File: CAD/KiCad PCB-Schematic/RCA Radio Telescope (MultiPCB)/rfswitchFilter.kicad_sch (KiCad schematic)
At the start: 15 parts, among them J10 FILTER_OUT, J9 ANT, U3 SKY13588-460LF, U4 SKY13588-460LF, U5 SN74AVC2T244DQER, U6 MIC5365-1.8YC5-TR, U7 MIC5365-3.3YC5-TR

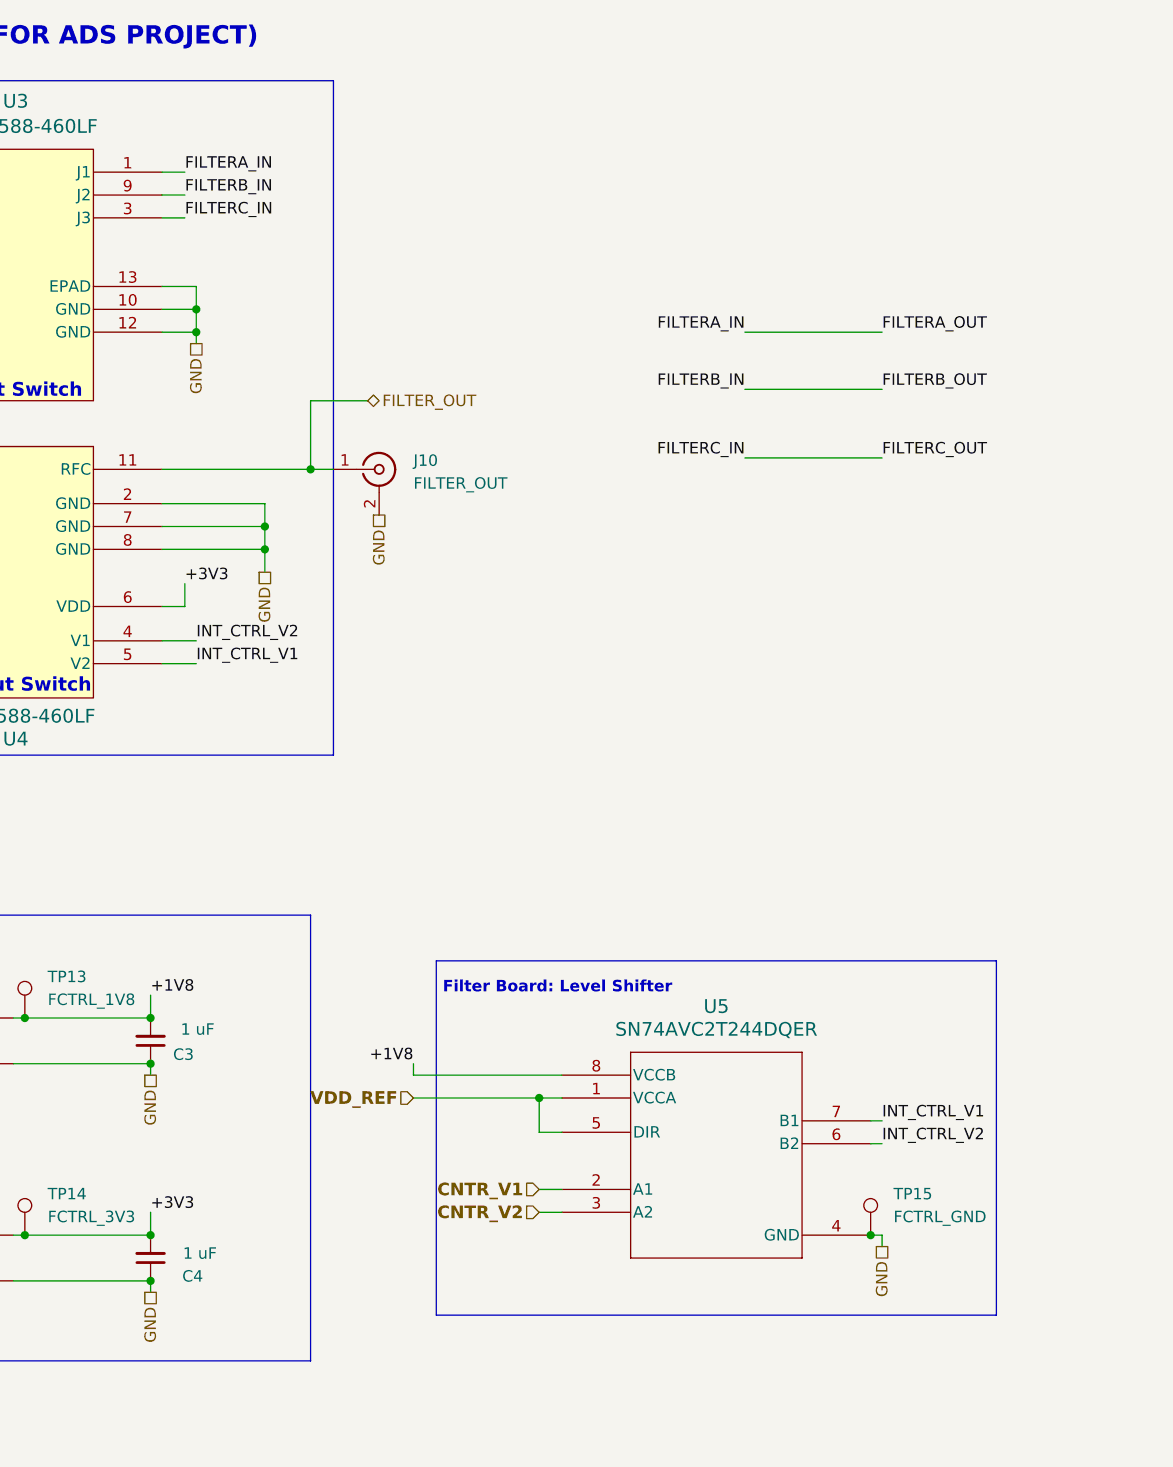
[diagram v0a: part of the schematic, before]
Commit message: Added 4 RF Board Designs into KiCAD project
- Added Matched SMD Filter Board, Matched Distributive Filter Board, RF Switch Filter Board, and kept original SMD Filter Board
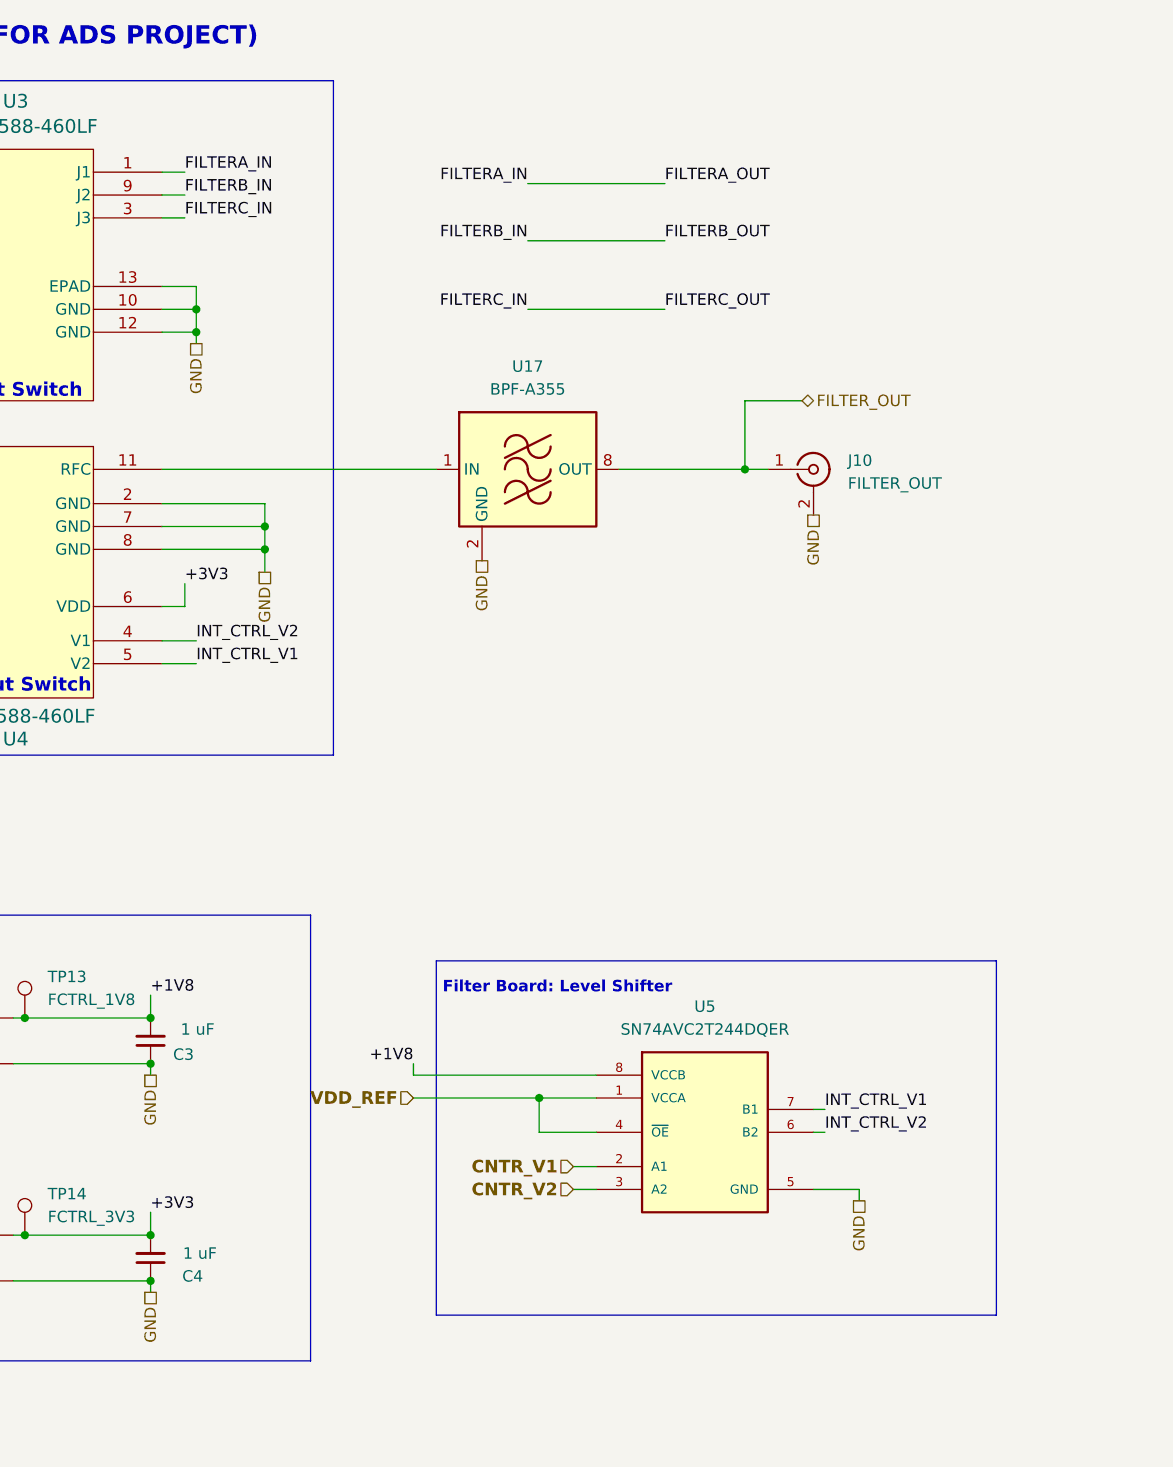
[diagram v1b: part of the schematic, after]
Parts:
- removed TP15: FCTRL_GND, Library:TestPoint_Pad_1.5x1.5mm_Edit, symbol Connector:TestPoint
- removed U5: SN74AVC2T244DQER, Library:SON35P140X100X40-8N, symbol Radio Telescope:SN74AVC2T45DCUR
- added U17: BPF-A355, RF_Mini-Circuits:Mini-Circuits_HQ1157, symbol RF_Filter:BPF-A355
- added U5: SN74AVC2T244DQER, Library:SON35P140X100X40-8N, symbol Radio Telescope:SN74AVC2T244DQER
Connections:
- net +1V8: now also U5.8 (VCCB)
- net CNTR_V1: now also U5.2 (A1)
- net CNTR_V2: now also U5.3 (A2)
- net FILTER_OUT: now also U17.8 (OUT); no longer U4.11 (RFC)
- net GND: now also U17.10 (GND), U17.11 (GND), U17.12 (GND), U17.13 (GND), U17.14 (GND), U17.2 (GND), U17.3 (GND), U17.4 (GND), U17.5 (GND), U17.6 (GND), U17.7 (GND), U17.9 (GND), U5.5 (GND)
- net INT_CTRL_V1: now also U5.7 (B1)
- net INT_CTRL_V2: now also U5.6 (B2)
- net VDD_REF: now also U5.1 (VCCA), U5.4 (~{OE})
- new net: U17.1 (IN), U4.11 (RFC)
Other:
- moved on the sheet: J10
